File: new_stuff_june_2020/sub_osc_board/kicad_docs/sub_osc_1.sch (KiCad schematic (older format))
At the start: 25 parts, among them Q1 MMBF4391, Q2 MMBF4391, U1 TL072, U2 TL072, U3 TL072, U7 40106, U8 4013

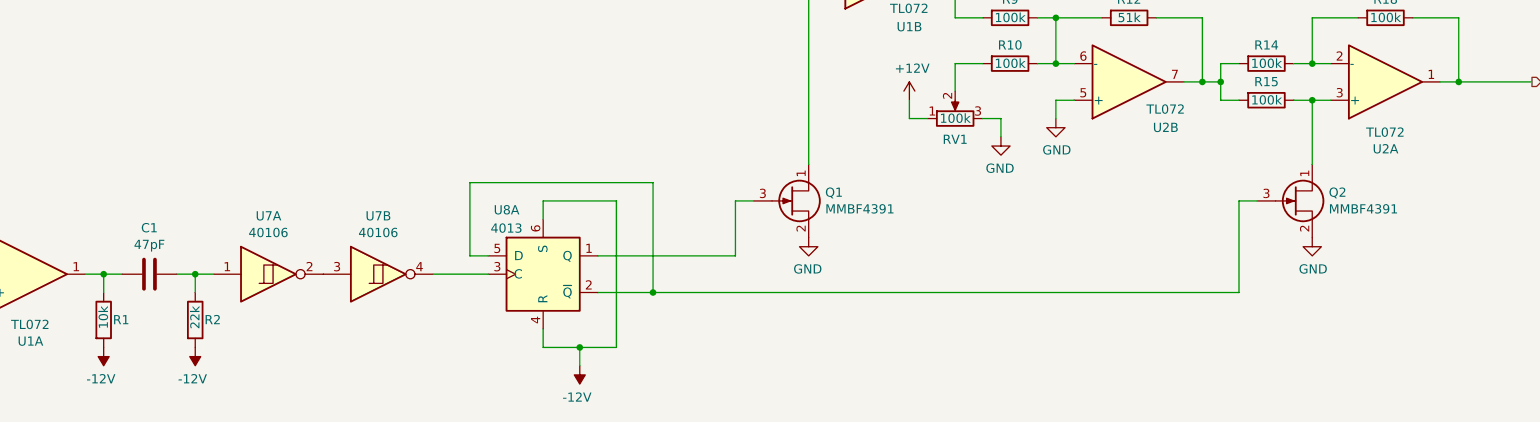
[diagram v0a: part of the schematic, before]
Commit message: change FETs and cap values
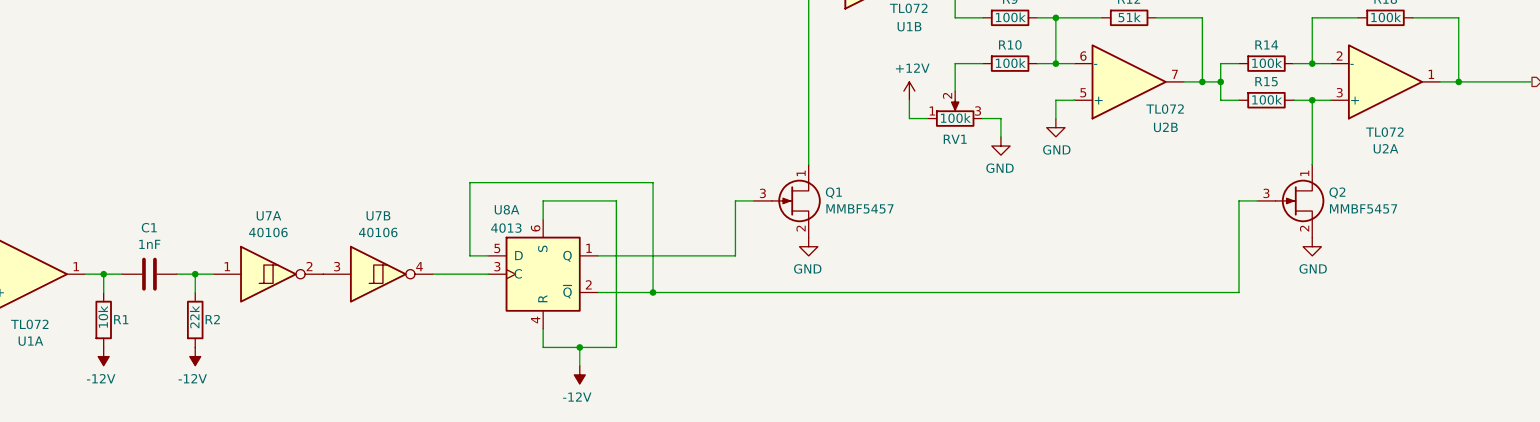
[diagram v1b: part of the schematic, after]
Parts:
- C1: value 47pF -> 1nF
- Q1, Q2: value MMBF4391 -> MMBF5457
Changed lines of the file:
@@
 AR Path="/5EE658F9/5EE669EE" Ref="C?"  Part="1"
 F 0 "C1" V 2098 4750 50  0000 C CNN
-F 1 "47pF" V 2189 4750 50  0000 C CNN
+F 1 "1nF" V 2189 4750 50  0000 C CNN
 F 2 "Capacitor_SMD:C_0805_2012Metric_Pad1.15x1.40mm_HandSolder" H 2388 4600 50  0001 C CNN
 F 3 "~" H 2350 4750 50  0001 C CNN
@@
 P 5850 4350
 F 0 "Q1" H 6040 4396 50  0000 L CNN
-F 1 "MMBF4391" H 6040 4305 50  0000 L CNN
+F 1 "MMBF5457" H 6040 4305 50  0000 L CNN
 F 2 "Package_TO_SOT_SMD:SOT-23_Handsoldering" H 6050 4275 50  0001 L CIN
 F 3 "https://www.onsemi.com/pub/Collateral/MMBF4391LT1-D.PDF" H 5850 4350 50  0001 L CNN
@@
 P 8600 4350
 F 0 "Q2" H 8790 4396 50  0000 L CNN
-F 1 "MMBF4391" H 8790 4305 50  0000 L CNN
+F 1 "MMBF5457" H 8790 4305 50  0000 L CNN
 F 2 "Package_TO_SOT_SMD:SOT-23_Handsoldering" H 8800 4275 50  0001 L CIN
 F 3 "https://www.onsemi.com/pub/Collateral/MMBF4391LT1-D.PDF" H 8600 4350 50  0001 L CNN
